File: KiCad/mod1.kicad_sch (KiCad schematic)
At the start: 67 parts, among them M1 Fan_4pin, M2 Fan_4pin, U1 ZD25Q64BSIGT

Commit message: Start moving components to module sheets to save sheets
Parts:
- added C163, C165, C166, C169: 100nF/50V, Capacitor_SMD:C_0402_1005Metric, symbol Device:C
- added C164: 10uF/10V, Capacitor_SMD:C_0603_1608Metric, symbol Device:C
- added C167, C168: 100uF/25V, Capacitor_SMD:CP_Elec_6.3x7.7, symbol Device:C_Polarized
- added C170: 560uF/25V, Capacitor_SMD:CP_Elec_6.3x7.7, symbol Device:C_Polarized
- added J13: SFF-8654-8i, EasyEDA2KiCAD:CONN-SMD_HBH2-74AT-1-UHR, symbol Custom:SFF-8654-8i
- added J14: RJE361882415, symbol Custom:1xRJ45+2xUSB3
- added J17: Bus_PCI_Express_x4, EasyEDA2KiCAD:PCIE-TH_AAA-PCI-161-K03, symbol Connector:Bus_PCI_Express_x4
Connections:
- net +12V: now also C165.1, C166.1, C167.1, C168.1, J17.A2 (+12V), J17.A3 (+12V), J17.B1 (+12V), J17.B2 (+12V), J17.B3 (+12V)
- net +3V3: now also C169.1, C170.1, J17.A10 (+3.3V), J17.A9 (+3.3V), J17.B8 (+3.3V)
- net +5V: now also J14.U1 (VBUS), J14.U10 (VBUS)
- net GND: now also C163.1, C164.1, C165.2, C166.2, C167.2, C168.2, C169.2, C170.2, J13.A1 (GND), J13.A10 (GND), J13.A13 (GND), J13.A16 (GND), J13.A19 (GND), J13.A22 (GND), J13.A25 (GND), J13.A28 (GND), J13.A31 (GND), J13.A34 (GND), J13.A37 (GND), J13.A4 (GND), J13.A7 (GND), J13.B1 (GND), J13.B10 (GND), J13.B12 (CPRSNTA#), J13.B13 (GND), J13.B16 (GND), J13.B19 (GND), J13.B22 (GND), J13.B25 (GND), J13.B28 (GND), J13.B30 (CPRSNTB#), J13.B31 (GND), J13.B34 (GND), J13.B37 (GND), J13.B4 (GND), J13.B7 (GND), J13.SH, J13.SH, J14.U13 (GND), J14.U16 (DRAIN), J14.U4 (GND), J14.U7 (DRAIN), J17.A1 (~{PRSNT1}), J17.A12 (GND), J17.A15 (GND), J17.A18 (GND), J17.A20 (GND), J17.A23 (GND), J17.A24 (GND), J17.A27 (GND), J17.A28 (GND), J17.A31 (GND), J17.A4 (GND), J17.B13 (GND), J17.B16 (GND), J17.B17 (~{PRSNT2}), J17.B18 (GND), J17.B21 (GND), J17.B22 (GND), J17.B25 (GND), J17.B26 (GND), J17.B29 (GND), J17.B31 (~{PRSNT2}), J17.B32 (GND), J17.B4 (GND), J17.B7 (GND)
- net FAN1_PWM: now reaches A1.2 (FAN1_PWM), R5.1
- net FAN2_TAC: now reaches A1.8 (FAN2_TAC), R4.1, R7.1
- net FAN2_PWM: now reaches A1.6 (FAN2_PWM), R6.1
- net FAN1_TAC: now reaches A1.4 (FAN1_TAC), R3.1
- new net +3V3SB: C163.2, C164.2, J17.B10 (3.3Vaux)
- new net NVME0_REFCLK+: J13.A11 (REFCLKA+)
- new net NVME0_REFCLK-: J13.A12 (REFCLKA-)
- new net NVME0_RX+: J13.A2 (PERp0)
- new net NVME0_RX-: J13.A3 (PERn0)
- new net NVME0_TX+: J13.B2 (PETp0)
- new net NVME0_TX-: J13.B3 (PETn0)
- new net NVME1_REFCLK+: J13.A29 (REFCLKB+)
- new net NVME1_REFCLK-: J13.A30 (REFCLKB-)
- new net NVME1_RX+: J13.A20 (PERp4)
- new net NVME1_RX-: J13.A21 (PERn4)
- new net NVME1_TX+: J13.B20 (PETp4)
- new net NVME1_TX-: J13.B21 (PETn4)
- new net PCIEX4_REFCLK+: J17.A13 (REFCLK+)
- new net PCIEX4_REFCLK-: J17.A14 (REFCLK-)
- new net PCIEX4_RX0+: J17.A16 (PERp0)
- new net PCIEX4_RX0-: J17.A17 (PERn0)
- new net PCIEX4_RX1+: J17.A21 (PERp1)
- new net PCIEX4_RX1-: J17.A22 (PERn1)
- new net PCIEX4_RX2+: J17.A25 (PERp2)
- new net PCIEX4_RX2-: J17.A26 (PERn2)
- new net PCIEX4_RX3+: J17.A29 (PERp3)
- new net PCIEX4_RX3-: J17.A30 (PERn3)
- new net PCIEX4_TX0+: J17.B14 (PETp0)
- new net PCIEX4_TX0-: J17.B15 (PETn0)
- new net PCIEX4_TX1+: J17.B19 (PETp1)
- new net PCIEX4_TX1-: J17.B20 (PETn1)
- new net PCIEX4_TX2+: J17.B23 (PETp2)
- new net PCIEX4_TX2-: J17.B24 (PETn2)
- new net PCIEX4_TX3+: J17.B27 (PETp3)
- new net PCIEX4_TX3-: J17.B28 (PETn3)
- new net RUSB0_D+: J14.U2 (D-)
- new net RUSB0_D-: J14.U3 (D+)
- new net RUSB0_SSRX+: J14.U5 (SSRX-)
- new net RUSB0_SSRX-: J14.U6 (SSRX+)
- new net RUSB0_SSTX+: J14.U8 (SSTX-)
- new net RUSB0_SSTX-: J14.U9 (SSTX+)
- new net RUSB1_D+: J14.U11 (D-)
- new net RUSB1_D-: J14.U12 (D+)
- new net RUSB1_SSRX+: J14.U14 (SSRX-)
- new net RUSB1_SSRX-: J14.U15 (SSRX+)
- new net RUSB1_SSTX+: J14.U17 (SSTX-)
- new net RUSB1_SSTX-: J14.U18 (SSTX+)
- new net SMB_CLK: J13.B26 (2W-CLKB), J13.B8 (2W-CLKA), J17.B5 (SMCLK)
- new net SMB_DATA: J13.B27 (2W-DATAB), J13.B9 (2W-DATAA), J17.B6 (SMDAT)
- new net ~{PCIE_RST}: J13.B11 (PERSTA#), J13.B29 (PERSTB#), J17.A11 (~{PERST})
- new net ~{PCIE_WAKE}: J13.A27 (CWAKEB#), J13.A9 (CWAKEA#), J17.B11 (~{WAKE})
- no-connect marks 83 -> 118
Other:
- moved on the sheet: A1, C1, C10, C11, C12, C13, C14, C15, C16, C17, C18, C19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

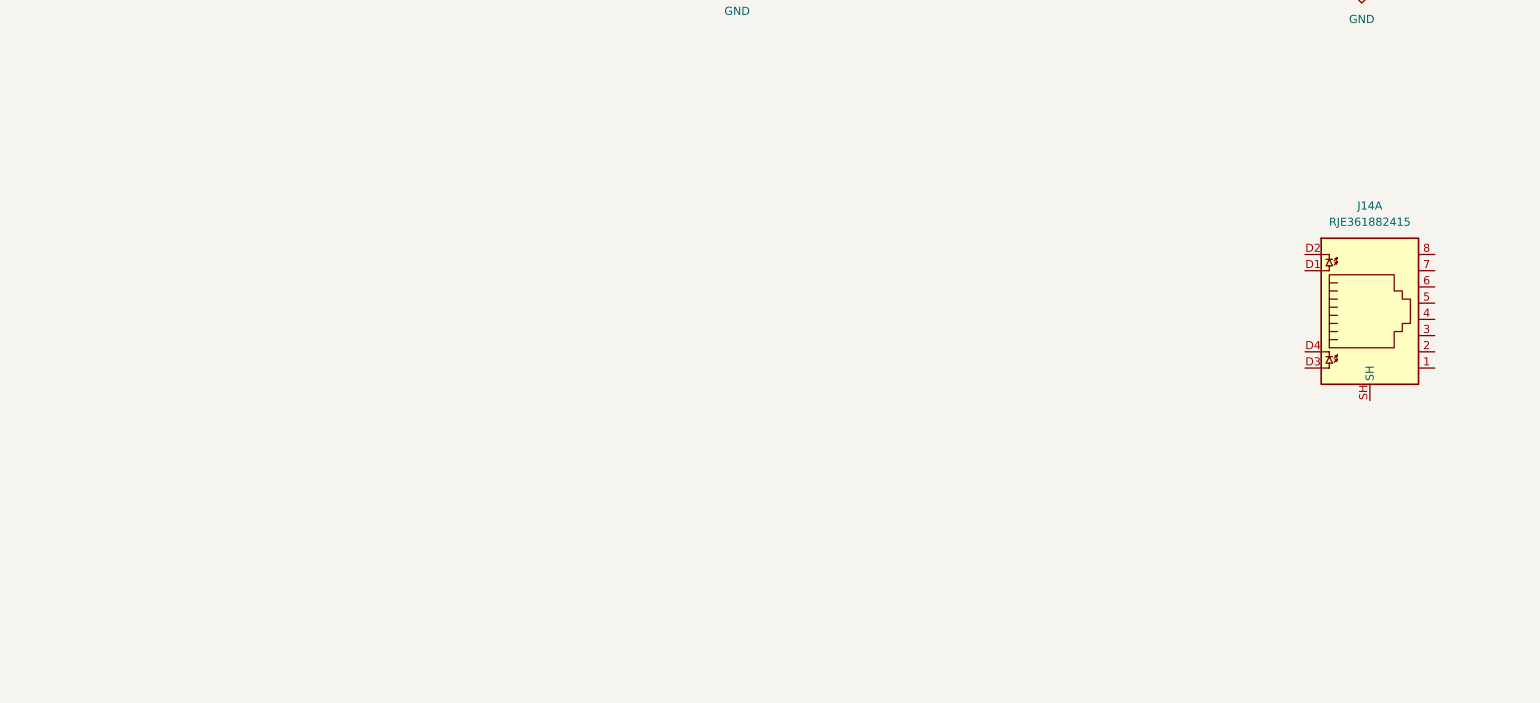
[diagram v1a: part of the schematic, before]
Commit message: Add RTL8125 to Module Sheet
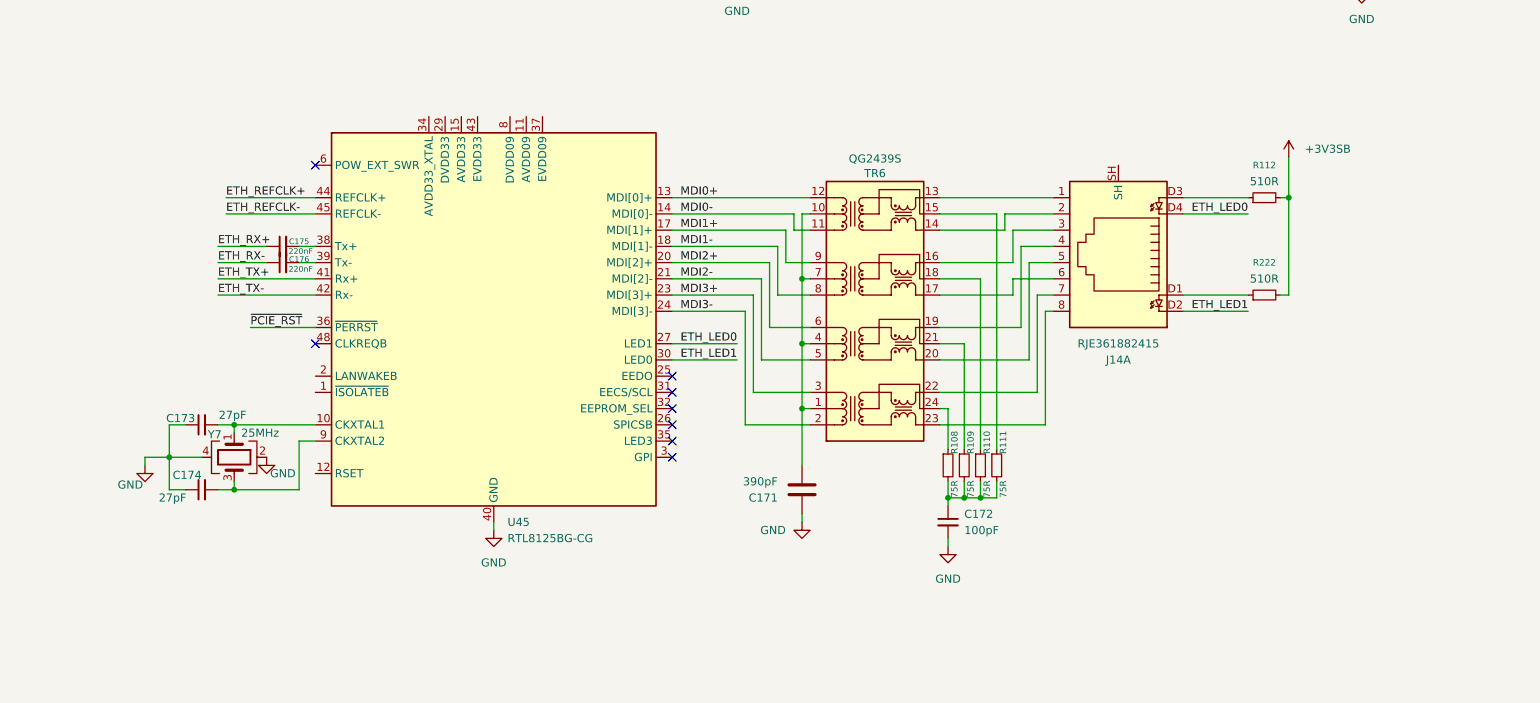
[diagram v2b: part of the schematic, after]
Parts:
- added C171: 390pF, Capacitor_SMD:C_0402_1005Metric, symbol Device:C
- added C172: 100pF, Capacitor_SMD:C_0402_1005Metric, symbol Device:C_Small
- added C173, C174: 27pF, Capacitor_SMD:C_0402_1005Metric, symbol Device:C_Small
- added C175, C176: 220nF, Capacitor_SMD:C_0402_1005Metric, symbol Device:C_Small
- added R108, R109, R110, R111: 75R, Resistor_SMD:R_0402_1005Metric, symbol Device:R_Small
- added R112, R222: 510R, Resistor_SMD:R_0402_1005Metric, symbol Device:R_Small
- added TR6: QG2439S, Custom:QG2439S, symbol Transformer:30F-51NL
- added U45: RTL8125BG-CG, Package_DFN_QFN:QFN-48-1EP_6x6mm_P0.4mm_EP4.2x4.2mm, symbol Custom:RTL8125BG-CG
- added Y7: 25MHz, Crystal:Crystal_SMD_3225-4Pin_3.2x2.5mm, symbol Device:Crystal_GND24
- J14: footprint (none) -> RJE361882145:AMPHENOL_RJE361882415
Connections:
- net +3V3SB: now also R112.2, R222.2
- net GND: now also C171.1, C172.2, C173.1, C174.1, U45.40 (GND), U45.49 (GND), Y7.2, Y7.4
- net ~{PCIE_RST}: now also U45.36 (~{PERRST})
- net at J14.1: now also TR6.13 (MX4-)
- net at J14.2: now also TR6.14 (MX4+)
- net at J14.3: now also TR6.16 (MX3-)
- net at J14.4: now also TR6.19 (MX2-)
- net at J14.5: now also TR6.20 (MX2+)
- net at J14.6: now also TR6.17 (MX3+)
- net at J14.7: now also TR6.22 (MX1-)
- net at J14.8: now also TR6.23 (MX1+)
- net at J14.D1: now also R222.1
- net ETH_LED1: now reaches J14.D2
- net ETH_LED1: now also U45.30 (EEDI/SDA)
- net at J14.D3: now also R112.1
- net ETH_LED0: now reaches J14.D4
- net ETH_LED0: now also U45.27 (EESK)
- new net: R109.1, TR6.21 (CT)
- new net: C172.1, R108.2, R109.2, R110.2, R111.2
- new net: C171.2, TR6.1 (CT), TR6.10 (CT), TR6.4 (CT), TR6.7 (CT)
- new net: R111.1, TR6.15 (CT)
- new net: R110.1, TR6.18 (CT)
- new net: R108.1, TR6.24 (CT)
- new net: C173.2, U45.10 (CKXTAL1), Y7.1
- new net: U45.11 (AVDD09), U45.16 (AVDD09), U45.22 (AVDD09)
- new net: U45.15 (AVDD33), U45.19 (AVDD33), U45.33 (AVDD33)
- new net: U45.28 (DVDD09), U45.47 (DVDD09), U45.8 (DVDD09)
- new net: U45.29 (DVDD33), U45.46 (DVDD33)
- new net: C175.2, U45.38 (Tx+)
- new net: C176.2, U45.39 (Tx-)
- new net: U45.4 (NC), U45.5 (NC), U45.7 (NC)
- new net: C174.2, U45.9 (CKXTAL2), Y7.3
- new net ETH_REFCLK+: U45.44 (REFCLK+)
- new net ETH_REFCLK-: U45.45 (REFCLK-)
- new net ETH_RX+: C175.1
- new net ETH_RX-: C176.1
- new net ETH_TX+: U45.41 (Rx+)
- new net ETH_TX-: U45.42 (Rx-)
- new net MDI0+: TR6.12 (TD4-), U45.13 (MDI[0]+)
- new net MDI0-: TR6.11 (TD4+), U45.14 (MDI[0]-)
- new net MDI1+: TR6.9 (TD3-), U45.17 (MDI[1]+)
- new net MDI1-: TR6.8 (TD3+), U45.18 (MDI[1]-)
- new net MDI2+: TR6.6 (TD2-), U45.20 (MDI[2]+)
- new net MDI2-: TR6.5 (TD2+), U45.21 (MDI[2]-)
- new net MDI3+: TR6.3 (TD1-), U45.23 (MDI[3]+)
- new net MDI3-: TR6.2 (TD1+), U45.24 (MDI[3]-)
- no-connect marks 118 -> 126
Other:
- moved on the sheet: J14A

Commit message: Finish RTL8125, Move HDMI
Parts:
- added C177, C180, C181, C182, C351, C352, C353, C356: 2.2uF, Capacitor_SMD:C_0402_1005Metric, symbol Device:C_Small
- added C178, C179, C357, C358, C359, C360, C361, C362, C363, C364, C365: 100nF, Capacitor_SMD:C_0402_1005Metric, symbol Device:C_Small
- added C347, C350, C354, C355: 10uF, Capacitor_SMD:C_0402_1005Metric, symbol Device:C_Small
- added C348, C349: 1uF, Capacitor_SMD:C_0402_1005Metric, symbol Device:C_Small
- added D22, D23: B0520W, Diode_SMD:D_SOD-123, symbol Device:D_Schottky
- added D24, D25, D26: SMF33A, Diode_SMD:D_SOD-123F, symbol Device:D_TVS
- added J18: HDMI_A, Connector_Video:HDMI_A_Molex_208658-1001_Horizontal, symbol Connector:HDMI_A
- added Q4, Q5, Q6, Q7: 2N7002, Package_TO_SOT_SMD:SOT-23, symbol Transistor_FET:Q_NMOS_GSD
- added R223: 4.7k, Resistor_SMD:R_0402_1005Metric, symbol Device:R_Small
- added R224, R225, R226, R227, R228, R229, R230, R231: 470R, Resistor_SMD:R_0402_1005Metric, symbol Device:R_Small
- added R232, R233, R235, R236: 2.2k, Resistor_SMD:R_0402_1005Metric, symbol Device:R_Small
- added R234: 1M, Resistor_SMD:R_0402_1005Metric, symbol Device:R_Small
- added R237: 1k, Resistor_SMD:R_0805_2012Metric, symbol Device:R_Small
- added R238: 22k, Resistor_SMD:R_0402_1005Metric, symbol Device:R_Small
- added U46, U47: H5VU25U, Package_DFN_QFN:Diodes_UDFN-10_1.0x2.5mm_P0.5mm, symbol Power_Protection:D3V3XA4B10LP
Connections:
- net +3V3: now also Q5.1 (G), Q6.1 (G), Q7.1 (G), R223.1, R234.1, R235.1, R236.1
- net +3V3SB: now also U45.15 (AVDD33), U45.19 (AVDD33), U45.29 (DVDD33), U45.33 (AVDD33), U45.34 (AVDD33_XTAL), U45.43 (EVDD33), U45.46 (DVDD33), C177.2, C178.2, C179.2, C180.2, C181.2, C182.2, C347.2, C348.2
- net +5V: now also D23.2 (A)
- net GND: now also J14.SH, C177.1, C178.1, C179.1, C180.1, C181.1, C182.1, C347.1, C348.1, C349.2, C350.2, C351.2, C352.2, C353.2, C354.2, C355.2, C356.2, C364.2, D24.1 (A1), D25.1 (A1), D26.1 (A1), J18.11 (CKS), J18.17 (GND), J18.2 (D2S), J18.5 (D1S), J18.8 (D0S), J18.SH, Q4.2 (S), R224.2, R225.2, R226.2, R227.2, R228.2, R229.2, R230.2, R231.2, R238.2, U46.3 (VSS), U46.8 (VSS), U47.3 (VSS), U47.8 (VSS)
- net MDI3-: now also C171.2, TR6.1 (CT), TR6.10 (CT), TR6.4 (CT), TR6.7 (CT)
- net ~{PCIE_WAKE}: now also U45.2 (LANWAKEB), R223.2
- net POWER_S0: now reaches U45.1 (~{ISOLATEB})
- net POWER_S0: now also A1.5 (SLS_S0), Q4.1 (G)
- net +0V95: now reaches U45.11 (AVDD09), U45.16 (AVDD09), U45.22 (AVDD09)
- net +0V95: now also U45.28 (DVDD09), U45.37 (EVDD09), U45.47 (DVDD09), U45.8 (DVDD09), C349.1, C350.1, C351.1, C352.1, C353.1, C354.1, C355.1, C356.1
- net at U45.6 (POW_EXT_SWR): now also D22.2 (A)
- net at D3.1 (K): now also Q4.3 (D); no longer A1.5 (SLS_S0)
- new net: Q7.3 (D), R237.1, R238.1
- new net: C360.2, J18.6 (D1-), R227.1, U46.4
- new net: C357.2, J18.1 (D2+), R224.1, U46.1
- new net: C358.2, J18.3 (D2-), R225.1, U46.2
- new net: C359.2, J18.4 (D1+), R226.1, U46.5
- new net: D25.2 (A2), J18.16 (SDA), Q6.3 (D), R233.2
- new net: C365.2, J18.12 (CK-), R231.1, U47.4
- new net: C362.2, J18.9 (D0-), R229.1, U47.2
- new net: C363.2, J18.10 (CK+), R230.1, U47.5
- new net: D24.2 (A2), J18.15 (SCL), Q5.3 (D), R232.2
- new net: D26.2 (A2), J18.19 (HPD), R237.2
- new net: C361.2, J18.7 (D0+), R228.1, U47.1
- new net +5VHDMI: C364.1, D23.1 (K), J18.18 (+5V), R232.1, R233.1
- new net 0V95_ENABLE: D22.1 (K)
- new net HDMI_HPD: Q7.2 (S), R234.2
- new net HDMI_SCL: Q5.2 (S), R236.2
- new net HDMI_SDA: Q6.2 (S), R235.2
- new net HDMI_TX0+: C357.1
- new net HDMI_TX0-: C358.1
- new net HDMI_TX1+: C359.1
- new net HDMI_TX1-: C360.1
- new net HDMI_TX2+: C361.1
- new net HDMI_TX2-: C362.1
- new net HDMI_TX3+: C363.1
- new net HDMI_TX3-: C365.1
- no-connect marks 126 -> 127
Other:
- moved on the sheet: C171, C172, C173, C174, C175, C176, D3, J13A, J13B, J14A, R108, R109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

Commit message: Add ESD Protection
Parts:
- removed D24, D25, D26: SMF33A, Diode_SMD:D_SOD-123F, symbol Device:D_TVS
- added R239: 2.49k, Resistor_SMD:R_0402_1005Metric, symbol Device:R_Small
- added U48, U49, U50, U51, U52, U53: H5VU25U, Package_DFN_QFN:Diodes_UDFN-10_1.0x2.5mm_P0.5mm, symbol Power_Protection:D3V3XA4B10LP
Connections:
- net ETH_LED0: now also U45.30 (EEDI/SDA); no longer U45.27 (EESK)
- net ETH_LED1: now also U45.27 (EESK); no longer U45.30 (EEDI/SDA)
- net GND: now also R239.2, U48.3 (VSS), U48.8 (VSS), U49.3 (VSS), U49.8 (VSS), U50.3 (VSS), U50.8 (VSS), U51.3 (VSS), U51.8 (VSS), U52.3 (VSS), U52.8 (VSS), U53.3 (VSS), U53.8 (VSS)
- net MDI0+: now also U49.1, U49.10 (NC)
- net MDI0-: now also U49.2, U49.9 (NC)
- net MDI1+: now also U49.4, U49.7 (NC)
- net MDI1-: now also U49.5, U49.6 (NC)
- net MDI2+: now also U50.1, U50.10 (NC)
- net MDI2-: now also U50.2, U50.9 (NC)
- net MDI3+: now also U50.4, U50.7 (NC)
- net MDI3-: now also U50.5, U50.6 (NC)
- net RUSB0_D+: now also U53.1, U53.10 (NC)
- net RUSB0_D-: now also U53.2, U53.9 (NC)
- net RUSB0_SSRX+: now also U51.1, U51.10 (NC)
- net RUSB0_SSRX-: now also U51.2, U51.9 (NC)
- net RUSB0_SSTX+: now also U51.4, U51.7 (NC)
- net RUSB0_SSTX-: now also U51.5, U51.6 (NC)
- net RUSB1_D+: now also U53.4, U53.7 (NC)
- net RUSB1_D-: now also U53.5, U53.6 (NC)
- net RUSB1_SSRX+: now also U52.1, U52.10 (NC)
- net RUSB1_SSRX-: now also U52.2, U52.9 (NC)
- net RUSB1_SSTX+: now also U52.4, U52.7 (NC)
- net RUSB1_SSTX-: now also U52.5, U52.6 (NC)
- net HDMI_D1-: now reaches C360.2, J18.6 (D1-), R227.1
- net HDMI_D1-: now also U46.5, U46.6 (NC); no longer U46.4
- net HDMI_D2+: now reaches C357.2, J18.1 (D2+), R224.1, U46.1
- net HDMI_D2+: now also U46.10 (NC)
- net HDMI_D2-: now reaches C358.2, J18.3 (D2-), R225.1, U46.2
- net HDMI_D2-: now also U46.9 (NC)
- net HDMI_D1+: now reaches C359.2, J18.4 (D1+), R226.1
- net HDMI_D1+: now also U46.4, U46.7 (NC); no longer U46.5
- net HDMI_SDAO: now reaches J18.16 (SDA), Q6.3 (D), R233.2
- net HDMI_SDAO: now also U48.2, U48.9 (NC)
- net HDMI_CK-: now reaches C365.2, J18.12 (CK-), R231.1
- net HDMI_CK-: now also U47.5, U47.6 (NC); no longer U47.4
- net HDMI_D0-: now reaches C362.2, J18.9 (D0-), R229.1, U47.2
- net HDMI_D0-: now also U47.9 (NC)
- net HDMI_CK+: now reaches C363.2, J18.10 (CK+), R230.1
- net HDMI_CK+: now also U47.4, U47.7 (NC); no longer U47.5
- net HDMI_SCLO: now reaches J18.15 (SCL), Q5.3 (D), R232.2
- net HDMI_SCLO: now also U48.1, U48.10 (NC)
- net HDMI_HPDO: now reaches J18.19 (HPD), R237.2
- net HDMI_HPDO: now also U48.5, U48.6 (NC)
- net HDMI_D0+: now reaches C361.2, J18.7 (D0+), R228.1, U47.1
- net HDMI_D0+: now also U47.10 (NC)
- net at U45.12 (RSET): now also R239.1
- no-connect marks 127 -> 128
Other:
- moved on the sheet: C171, C172, C173, C174, C175, C176, C177, C178, C179, C180, C181, C182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

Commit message: Start connecting module
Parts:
- removed C15, C16, C17, C18: 10nF, Capacitor_SMD:C_0402_1005Metric, symbol Device:C_Small
- removed C22, C23: 100pF, Capacitor_SMD:C_0402_1005Metric, symbol Device:C_Small
- removed C24, C25: 100nF, Capacitor_SMD:C_0402_1005Metric, symbol Device:C_Small
- removed C26, C27, C30, C31: 330nF, Capacitor_SMD:C_0402_1005Metric, symbol Device:C_Small
- removed C28, C29, C32, C33: 220nF, Capacitor_SMD:C_0402_1005Metric, symbol Device:C_Small
- removed R26: 100k, Resistor_SMD:R_0402_1005Metric, symbol Device:R_Small
- C11, C12, C13, C14: value 10nF -> 220nF
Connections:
- net ETH.Rx0+ is gone; now on net ETH_RX+: A1.64 (HSIO6_RX+)
- net ETH.Rx0- is gone; now on net ETH_RX-: A1.66 (HSIO6_RX-)
- net ETH.Tx0+ is gone; now on net ETH_TX+: C19.1
- net ETH.Tx0- is gone; now on net ETH_TX-: C20.1
- net NVME.Rx0+ is gone; now on net PCIEX4_RX0+: A1.40 (HSIO8_RX+)
- net NVME.Rx0- is gone; now on net PCIEX4_RX0-: A1.42 (HSIO8_RX-)
- net NVME.Rx1+ is gone; now on net PCIEX4_RX1+: A1.46 (HSIO9_RX+)
- net NVME.Rx1- is gone; now on net PCIEX4_RX1-: A1.48 (HSIO9_RX-)
- net NVME.Tx0+ is gone; now on net PCIEX4_TX0+: C7.1
- net NVME.Tx0- is gone; now on net PCIEX4_TX0-: C8.1
- net NVME.Tx1+ is gone; now on net PCIEX4_TX1+: C9.1
- net NVME.Tx1- is gone; now on net PCIEX4_TX1-: C10.1
- net REAR_DISPLAY.HPD is gone; now on net HDMI_HPD: A1.183 (DDIB_HPD)
- net REAR_DISPLAY.SCL is gone; now on net HDMI_SCL: A1.171 (DDIB_DDC_SCL)
- net REAR_DISPLAY.SDA is gone; now on net HDMI_SDA: A1.169 (DDIB_DDC_SDA)
- net REAR_DISPLAY.Tx0+ is gone; now on net HDMI_TX0+: A1.217 (DDIB_TX0+)
- net REAR_DISPLAY.Tx0- is gone; now on net HDMI_TX0-: A1.215 (DDIB_TX0-)
- net REAR_DISPLAY.Tx1+ is gone; now on net HDMI_TX1+: A1.211 (DDIB_TX1+)
- net REAR_DISPLAY.Tx1- is gone; now on net HDMI_TX1-: A1.209 (DDIB_TX1-)
- net REAR_DISPLAY.Tx2+ is gone; now on net HDMI_TX2+: A1.205 (DDIB_TX2+)
- net REAR_DISPLAY.Tx2- is gone; now on net HDMI_TX2-: A1.203 (DDIB_TX2-)
- net REAR_DISPLAY.Tx3+ is gone; now on net HDMI_TX3+: A1.199 (DDIB_TX3+)
- net REAR_DISPLAY.Tx3- is gone; now on net HDMI_TX3-: A1.197 (DDIB_TX3-)
- net RUSB_1.D+ is gone; now on net RUSB0_D+: A1.69 (USB2_P1+)
- net RUSB_1.D- is gone; now on net RUSB0_D-: A1.67 (USB2_P1-)
- net RUSB_1.SS_Rx1+ is gone; now on net RUSB0_SSRX+: A1.16 (HSIO0_RX+)
- net RUSB_1.SS_Rx1- is gone; now on net RUSB0_SSRX-: A1.18 (HSIO0_RX-)
- net RUSB_1.SS_Tx1+ is gone; now on net RUSB0_SSTX+: C3.1
- net RUSB_1.SS_Tx1- is gone; now on net RUSB0_SSTX-: C4.1
- net RUSB_2.D+ is gone; now on net RUSB1_D+: A1.75 (USB2_P2+)
- net RUSB_2.D- is gone; now on net RUSB1_D-: A1.73 (USB2_P2-)
- net RUSB_2.SS_Rx1+ is gone; now on net RUSB1_SSRX+: A1.22 (HSIO1_RX+)
- net RUSB_2.SS_Rx1- is gone; now on net RUSB1_SSRX-: A1.24 (HSIO1_RX-)
- net RUSB_2.SS_Tx1+ is gone; now on net RUSB1_SSTX+: C5.1
- net RUSB_2.SS_Tx1- is gone; now on net RUSB1_SSTX-: C6.1
- net SATA1.Rx+ is gone; now on net PCIEX4_TX3+: C13.1
- net SATA1.Rx- is gone; now on net PCIEX4_TX3-: C14.1
- net SATA1.Tx+ is gone; now on net PCIEX4_TX2+: C11.1
- net SATA1.Tx- is gone; now on net PCIEX4_TX2-: C12.1
- net TYPE_C_HEADER.SBU1 is gone; now on net GND: R25.1
- net PCIEX4_RX2+: now also A1.52 (HSIO10_RX+)
- net PCIEX4_RX2-: now also A1.54 (HSIO10_RX-)
- net PCIEX4_RX3+: now also A1.58 (HSIO11_RX+)
- net PCIEX4_RX3-: now also A1.60 (HSIO11_RX-)
- net at C13.2: now also A1.55 (HSIO11_TX+); no longer A1.52 (HSIO10_RX+)
- net at A1.57 (HSIO11_TX-): now also C14.2
- net at A1.173 (TCP1_DDC_SDA): no longer R25.2
- net TYPE_C_HPD: no longer names the net of A1.185 (TCP1_HPD)
- net TYPE_C_HPD: now also R25.2
